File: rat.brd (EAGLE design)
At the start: 102.5 x 80 mm, 64 parts, among them J1 B2B-PH-K-S(LF)(SN), J2 B2B-PH-K-S(LF)(SN), J3 PPTC041LFBN-RC, J4 PPTC081LFBN-RCCONN_PPTC081LFB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, Q1A SFH_313_FA-3/4, Q1B SFH_313_FA-3/4, Q1C SFH_313_FA-3/4, Q1D SFH_313_FA-3/4, Q2A Q2, Q2B Q2, Q2C Q2, Q2D Q2, U1 L293DD, U2 LD1117D33CTR, U3 STM32F205RGT6

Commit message: Some Routing Done
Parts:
- moved R3A 25.3 mm to (78.1, 67.9), turned to 180 degrees
- moved R3C 23.4 mm to (80.0, 29.2), turned to 270 degrees
- moved C13 21.5 mm to (35.6, 9.53), turned to 0 degrees
- moved S1 18.7 mm to (19.7, 31.8), turned to 180 degrees
- moved R5 14.3 mm to (50.2, 22.7), turned to 90 degrees
- moved RIGHT 13.2 mm to (56.4, 72.8), turned to 180 degrees
- moved R2C 10.6 mm to (47.6, 23.2)
- moved R6 7.01 mm to (61.6, 51.4), turned to 90 degrees
- moved C11 6.35 mm to (63.5, 45.7), turned to 180 degrees
- moved R4C 5.85 mm to (87.6, 27.3), turned to 180 degrees
- moved C8D 5.75 mm to (18.4, 61.6), turned to 90 degrees
- moved Q2D 5.68 mm to (76.2, 15.2)
- moved R1D 5.68 mm to (43.2, 22.9), turned to 90 degrees
- moved R3D 5.12 mm to (66.7, 36.8), turned to 180 degrees
- moved R4D 4.02 mm to (68.6, 15.2), turned to 90 degrees
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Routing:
- net N$14: track 0.00 -> 61.2 mm, vias 0 -> 2
- net PC7: track 0.00 -> 60.6 mm
- net VBAT: track 0.00 -> 59.9 mm
- net VCC: track 0.00 -> 53.9 mm
- net PB6: track 0.00 -> 36.2 mm, vias 0 -> 2
- net N$8: track 0.00 -> 34.9 mm
- net PB8: track 0.00 -> 32.7 mm, vias 0 -> 2
- net N$17: track 0.00 -> 28.4 mm
- net N$2: track 0.00 -> 26.4 mm
- net PB10: track 0.00 -> 25.7 mm
- net PB11: track 0.00 -> 25.5 mm
- net N$5: track 0.00 -> 22.7 mm
- net N$3: track 0.00 -> 22.1 mm
- net PB7: track 0.00 -> 18.7 mm, vias 0 -> 2
- net N$4: track 0.00 -> 18.6 mm
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- added copper zone on layer 1, net VCC
- removed copper zone on layer 1, net VBAT

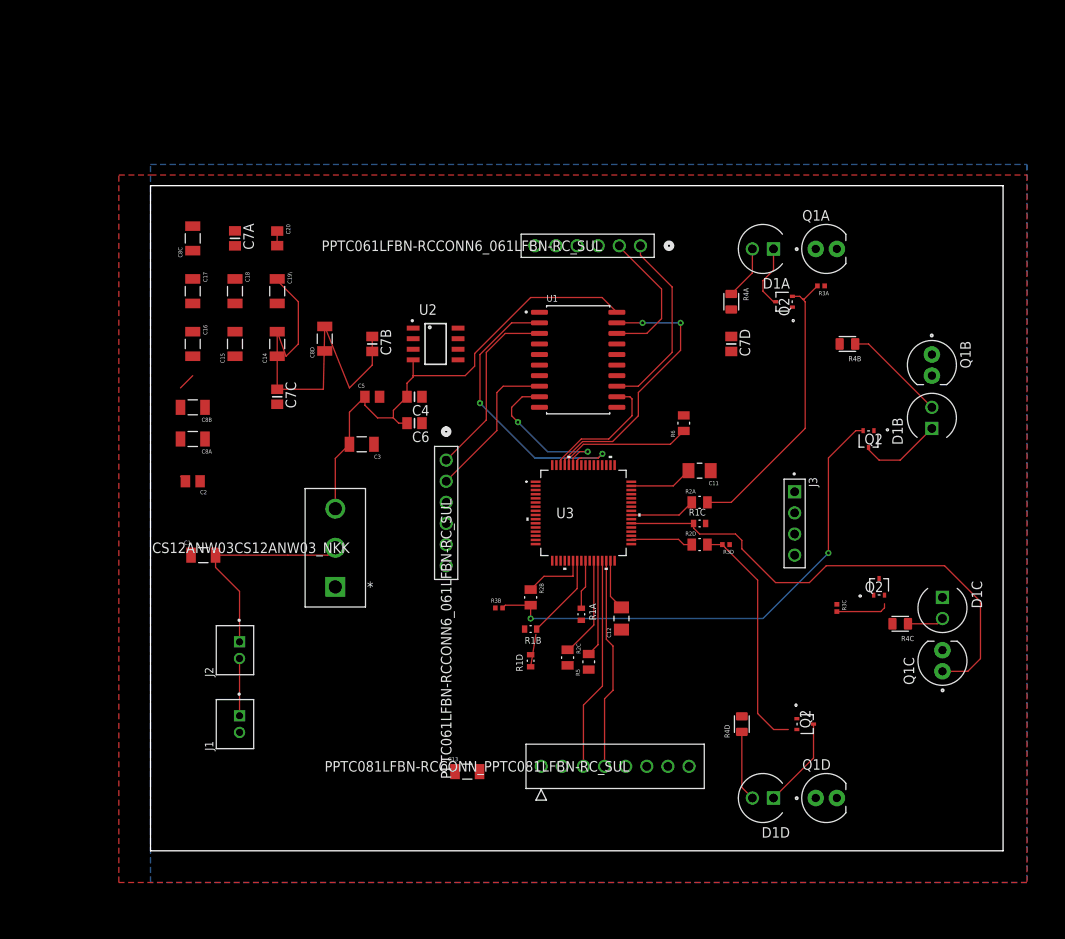
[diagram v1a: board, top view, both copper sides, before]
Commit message: Airwires eliminated
Restriction problems still remain; not sure why I can't route under components
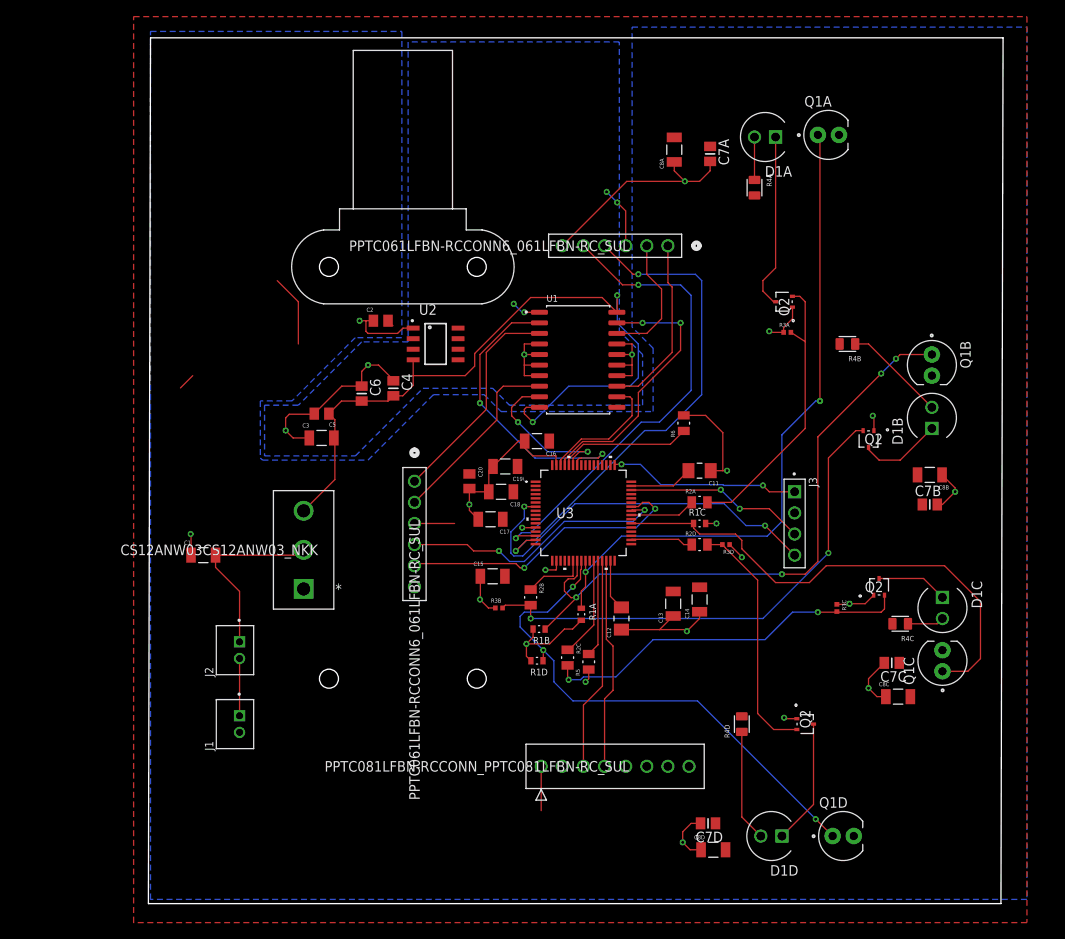
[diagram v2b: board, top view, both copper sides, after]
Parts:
- added U$1, U$2: MOTOR, micromouseMotors:MOTOR
- moved C8C 101.2 mm to (87.4, 18.5), turned to 0 degrees
- moved C8B 89.0 mm to (91.2, 45.2)
- moved C7C 80.5 mm to (86.6, 22.6), turned to 180 degrees
- moved C8D 77.2 mm to (65.2, 0.13), turned to 0 degrees
- moved C7B 69.8 mm to (91.2, 41.7), turned to 0 degrees
- moved C8A 67.6 mm to (60.5, 84.3), turned to 90 degrees
- moved C14 59.4 mm to (63.5, 30.2)
- moved C7A 58.0 mm to (64.8, 83.8)
- moved C7D 57.7 mm to (64.5, 3.30), turned to 180 degrees
- moved C17 45.1 mm to (38.4, 39.9), turned to 180 degrees
- moved C16 43.0 mm to (43.9, 49.3), turned to 180 degrees
- moved C15 41.7 mm to (38.6, 33.0), turned to 0 degrees
- moved C18 40.1 mm to (39.6, 43.2), turned to 180 degrees
- moved C20 37.2 mm to (35.8, 44.5)
- moved C19\ 34.6 mm to (40.1, 46.2), turned to 180 degrees
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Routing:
- net GND: track 0.00 -> 141.6 mm, vias 0 -> 20
- net PC5: track 5.93 -> 80.9 mm, vias 0 -> 2
- net PA7: track 10.2 -> 75.5 mm, vias 0 -> 4
- net PA1: track 0.00 -> 60.2 mm, vias 0 -> 2
- net PC4: track 3.95 -> 63.4 mm, vias 0 -> 3
- net PA0: track 0.00 -> 57.8 mm, vias 0 -> 2
- net NRST: track 0.00 -> 47.1 mm, vias 0 -> 2
- net MGND: track 0.00 -> 44.4 mm, vias 0 -> 4
- net N$10: track 6.41 -> 45.0 mm, vias 0 -> 2
- net PA9: track 0.00 -> 35.6 mm, vias 0 -> 2
- net PA8: track 0.00 -> 32.8 mm, vias 0 -> 2
- net VBAT: track 59.9 -> 90.4 mm, vias 0 -> 2
- net SWCLK: track 0.00 -> 23.1 mm, vias 0 -> 2
- net SWDIO: track 0.00 -> 21.9 mm, vias 0 -> 2
- net VCC: track 53.9 -> 32.7 mm, vias 0 -> 5
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- added copper zone on layer 16, net MGND
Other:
- board size 102.5 x 80 mm -> 102.8 x 104.1 mm

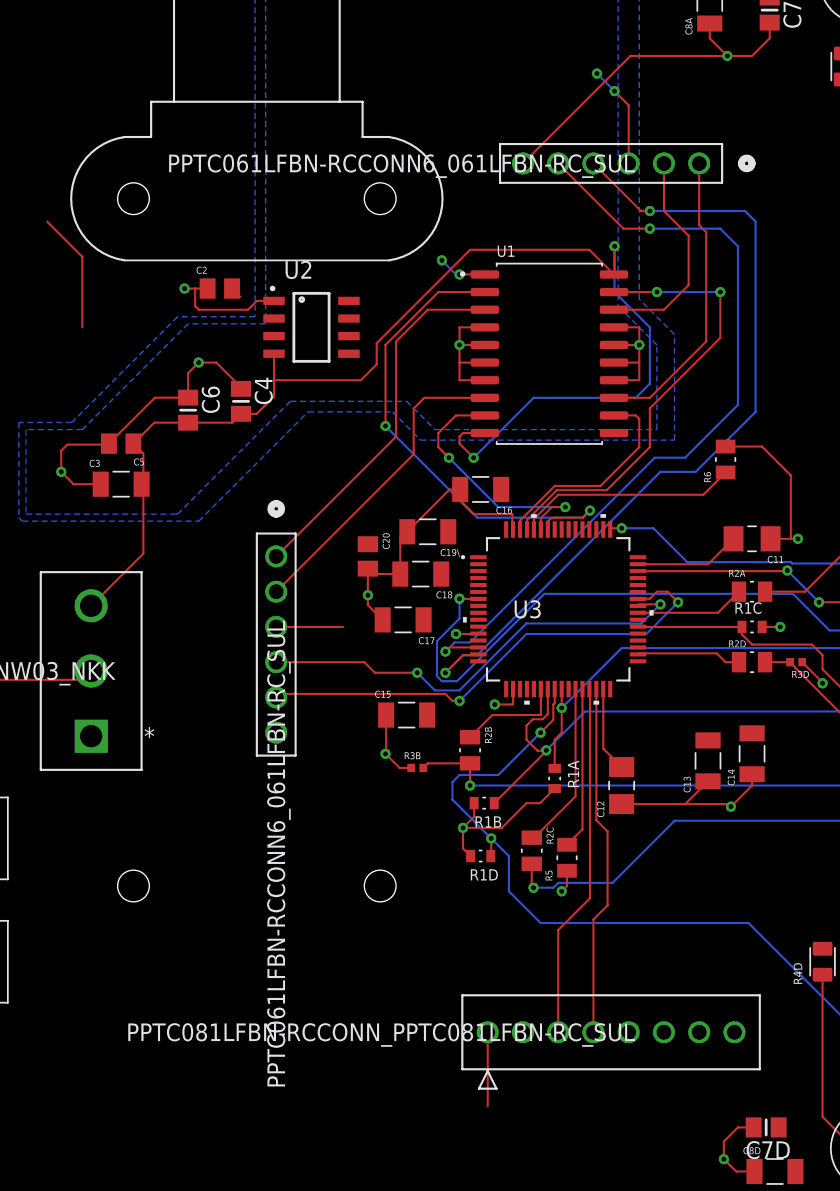
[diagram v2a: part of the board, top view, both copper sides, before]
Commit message: Made Power Signals 45mil Trace
Still need to make analog signals 15mil trace
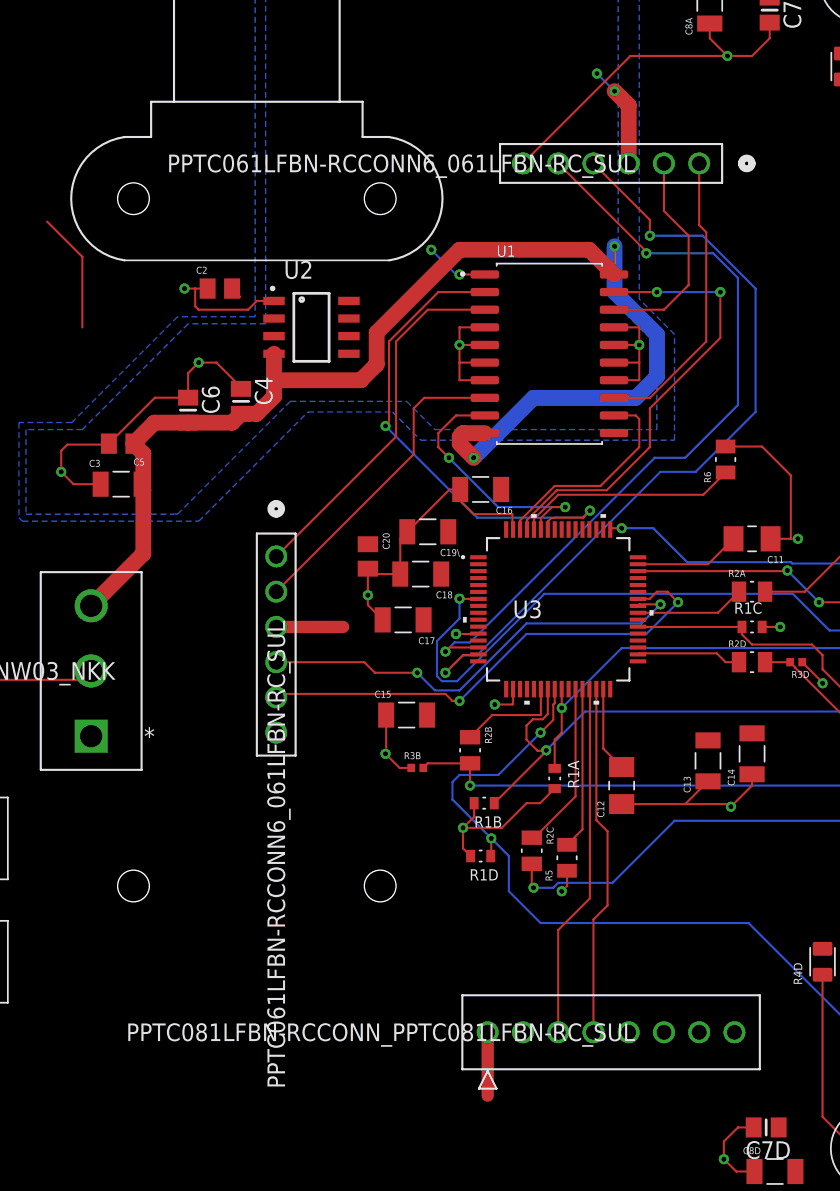
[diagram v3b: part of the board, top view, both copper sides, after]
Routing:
- net PA1: track 60.2 -> 58.0 mm
- net PA0: track 57.8 -> 56.5 mm
- net VBAT: track 90.4 -> 91.3 mm
- net VCC: track 32.7 -> 33.0 mm, vias 5 -> 4
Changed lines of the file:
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@@
 <via x="42.418" y="64.77" extent="1-16" drill="0.35"/>
 <wire x1="42.418" y1="64.77" x2="42.164" y2="64.77" width="0.1524" layer="16"/>
-<wire x1="42.164" y1="64.77" x2="41.148" y2="65.786" width="0.1524" layer="16"/>
-<via x="41.148" y="65.786" extent="1-16" drill="0.35"/>
-<wire x1="54.61" y1="72.771" x2="54.61" y2="76.962" width="0.1524" layer="1"/>
-<wire x1="54.61" y1="76.962" x2="53.594" y2="77.978" width="0.1524" layer="1"/>
+<wire x1="42.164" y1="64.77" x2="40.386" y2="66.548" width="0.1524" layer="16"/>
+<via x="40.386" y="66.548" extent="1-16" drill="0.35"/>
+<wire x1="54.61" y1="72.771" x2="54.61" y2="76.962" width="1.143" layer="1"/>
+<wire x1="54.61" y1="76.962" x2="53.594" y2="77.978" width="1.143" layer="1"/>
 <via x="53.594" y="77.978" extent="1-16" drill="0.35"/>
 <wire x1="53.594" y1="77.978" x2="52.324" y2="79.248" width="0.1524" layer="16"/>
 <via x="52.324" y="79.248" extent="1-16" drill="0.35"/>
-<via x="44.45" y="10.16" extent="1-16" drill="0.35"/>
-<wire x1="44.45" y1="10.16" x2="44.45" y2="4.826" width="0.1524" layer="1"/>
-<wire x1="29.21" y1="39.37" x2="34.036" y2="39.37" width="0.1524" layer="1"/>
+<wire x1="29.21" y1="39.37" x2="34.036" y2="39.37" width="0.889" layer="1"/>
+<wire x1="44.45" y1="10.16" x2="44.45" y2="5.588" width="0.889" layer="1"/>
 </signal>
 <signal name="N$3">
@@
 <contactref element="U3" pad="58"/>
 <wire x1="44.24" y1="63.5" x2="40.894" y2="63.5" width="0.1524" layer="1"/>
-<wire x1="40.894" y1="63.5" x2="37.084" y2="59.69" width="0.1524" layer="1"/>
-<wire x1="37.084" y1="59.69" x2="37.084" y2="53.848" width="0.1524" layer="1"/>
+<wire x1="40.894" y1="63.5" x2="37.338" y2="59.944" width="0.1524" layer="1"/>
+<wire x1="37.338" y1="59.944" x2="37.338" y2="54.102" width="0.1524" layer="1"/>
+<wire x1="37.338" y1="54.102" x2="37.084" y2="53.848" width="0.1524" layer="1"/>
 <wire x1="49.0329125" y1="47.2155" x2="49.2475" y2="47.2155" width="0.1524" layer="1"/>
 <wire x1="49.2475" y1="47.2155" x2="49.276" y2="47.244" width="0.1524" layer="1"/>
@@
 <contactref element="C4" pad="2"/>
 <contactref element="C6" pad="2"/>
-<wire x1="19.633434375" y1="49.2246125" x2="19.633434375" y2="44.652434375" width="0.1524" layer="1"/>
-<wire x1="15.875" y1="40.894" x2="19.633434375" y2="44.652434375" width="0.1524" layer="1"/>
+<wire x1="19.633434375" y1="49.2246125" x2="19.633434375" y2="44.652434375" width="1.143" layer="1"/>
+<wire x1="15.875" y1="40.894" x2="19.633434375" y2="44.652434375" width="1.143" layer="1"/>
 <wire x1="19.633434375" y1="49.2246125" x2="19.509" y2="49.657" width="0.1524" layer="1"/>
-<wire x1="29.05" y1="55.974" x2="27.802" y2="54.726" width="0.1524" layer="1"/>
-<wire x1="26.67" y1="54.726" x2="27.802" y2="54.726" width="0.1524" layer="1"/>
-<wire x1="53.55" y1="64.77" x2="51.772" y2="66.548" width="0.1524" layer="1"/>
-<wire x1="51.772" y1="66.548" x2="43.18" y2="66.548" width="0.1524" layer="1"/>
-<wire x1="43.18" y1="66.548" x2="36.449" y2="59.817" width="0.1524" layer="1"/>
-<wire x1="36.449" y1="59.817" x2="36.449" y2="58.293" width="0.1524" layer="1"/>
-<wire x1="35.306" y1="57.15" x2="29.05" y2="57.15" width="0.1524" layer="1"/>
-<wire x1="36.449" y1="58.293" x2="35.306" y2="57.15" width="0.1524" layer="1"/>
-<wire x1="26.67" y1="54.726" x2="26.035" y2="54.091" width="0.1524" layer="1"/>
-<wire x1="26.035" y1="54.091" x2="22.86" y2="54.091" width="0.1524" layer="1"/>
-<wire x1="18.914" y1="52.578" x2="20.427" y2="54.091" width="0.1524" layer="1"/>
-<wire x1="20.427" y1="54.091" x2="22.86" y2="54.091" width="0.1524" layer="1"/>
-<wire x1="18.914" y1="52.578" x2="19.633434375" y2="51.858565625" width="0.1524" layer="1"/>
-<wire x1="19.633434375" y1="51.858565625" x2="19.633434375" y2="49.2246125" width="0.1524" layer="1"/>
-<wire x1="29.05" y1="59.055" x2="29.05" y2="57.15" width="0.1524" layer="1"/>
-<wire x1="29.05" y1="57.15" x2="29.05" y2="55.974" width="0.1524" layer="1"/>
-<wire x1="44.24" y1="53.34" x2="42.672" y2="53.34" width="0.1524" layer="1"/>
-<wire x1="42.672" y1="53.34" x2="42.418" y2="53.086" width="0.1524" layer="1"/>
+<wire x1="29.05" y1="55.974" x2="27.802" y2="54.726" width="1.143" layer="1"/>
+<wire x1="26.67" y1="54.726" x2="27.802" y2="54.726" width="1.143" layer="1"/>
+<wire x1="53.55" y1="64.77" x2="51.772" y2="66.548" width="1.143" layer="1"/>
+<wire x1="51.772" y1="66.548" x2="42.418" y2="66.548" width="1.143" layer="1"/>
+<wire x1="42.418" y1="66.548" x2="36.449" y2="60.579" width="1.143" layer="1"/>
+<wire x1="36.449" y1="60.579" x2="36.449" y2="58.293" width="1.143" layer="1"/>
+<wire x1="35.306" y1="57.15" x2="29.05" y2="57.15" width="1.143" layer="1"/>
+<wire x1="36.449" y1="58.293" x2="35.306" y2="57.15" width="1.143" layer="1"/>
+<wire x1="26.67" y1="54.726" x2="26.035" y2="54.091" width="1.143" layer="1"/>
+<wire x1="26.035" y1="54.091" x2="22.86" y2="54.091" width="1.143" layer="1"/>
+<wire x1="18.914" y1="52.578" x2="20.427" y2="54.091" width="1.143" layer="1"/>
+<wire x1="20.427" y1="54.091" x2="22.86" y2="54.091" width="1.143" layer="1"/>
+<wire x1="18.914" y1="52.578" x2="19.633434375" y2="51.858565625" width="1.143" layer="1"/>
+<wire x1="19.633434375" y1="51.858565625" x2="19.633434375" y2="49.2246125" width="1.143" layer="1"/>
+<wire x1="29.05" y1="59.055" x2="29.05" y2="57.15" width="1.143" layer="1"/>
+<wire x1="29.05" y1="57.15" x2="29.05" y2="55.974" width="1.143" layer="1"/>
+<wire x1="44.24" y1="53.34" x2="42.672" y2="53.34" width="1.143" layer="1"/>
+<wire x1="42.672" y1="53.34" x2="42.418" y2="53.086" width="1.143" layer="1"/>
 <wire x1="42.418" y1="53.086" x2="42.418" y2="52.578" width="0.1524" layer="1"/>
-<wire x1="42.418" y1="52.578" x2="43.434" y2="51.562" width="0.1524" layer="1"/>
+<wire x1="42.418" y1="52.578" x2="43.434" y2="51.562" width="1.143" layer="1"/>
 <via x="43.434" y="51.562" extent="1-16" drill="0.35"/>
-<wire x1="43.434" y1="51.562" x2="47.752" y2="55.88" width="0.1524" layer="16"/>
+<wire x1="43.434" y1="51.562" x2="47.752" y2="55.88" width="1.143" layer="16"/>
 <via x="53.594" y="66.802" extent="1-16" drill="0.35"/>
 <wire x1="53.594" y1="66.802" x2="53.594" y2="64.814" width="0.1524" layer="1"/>
 <wire x1="53.594" y1="64.814" x2="53.55" y2="64.77" width="0.1524" layer="1"/>
-<wire x1="55.118" y1="55.88" x2="56.134" y2="56.896" width="0.1524" layer="16"/>
-<wire x1="56.134" y1="56.896" x2="56.134" y2="60.96" width="0.1524" layer="16"/>
-<wire x1="53.594" y1="63.5" x2="53.594" y2="66.802" width="0.1524" layer="16"/>
-<wire x1="47.752" y1="55.88" x2="55.118" y2="55.88" width="0.1524" layer="16"/>
-<wire x1="56.134" y1="60.96" x2="53.594" y2="63.5" width="0.1524" layer="16"/>
+<wire x1="55.118" y1="55.88" x2="56.642" y2="57.404" width="1.143" layer="16"/>
+<wire x1="56.642" y1="57.404" x2="56.642" y2="60.452" width="1.143" layer="16"/>
+<wire x1="53.594" y1="63.5" x2="53.594" y2="66.802" width="1.143" layer="16"/>
+<wire x1="47.752" y1="55.88" x2="55.118" y2="55.88" width="1.143" layer="16"/>
+<wire x1="56.642" y1="60.452" x2="53.594" y2="63.5" width="1.143" layer="16"/>
 </signal>
 <signal name="N$26">
@@
 <wire x1="42.0652" y1="38.2552" x2="43.17735" y2="38.2552" width="0.1524" layer="16"/>
 <wire x1="43.17735" y1="38.2552" x2="56.48415" y2="51.562" width="0.1524" layer="16"/>
-<wire x1="62.484" y1="55.372" x2="58.674" y2="51.562" width="0.1524" layer="16"/>
-<via x="56.134" y="68.072" extent="1-16" drill="0.35"/>
-<wire x1="49.53" y1="72.771" x2="54.229" y2="68.072" width="0.1524" layer="1"/>
-<wire x1="54.229" y1="68.072" x2="56.134" y2="68.072" width="0.1524" layer="1"/>
-<wire x1="61.214" y1="68.072" x2="62.484" y2="66.802" width="0.1524" layer="16"/>
-<wire x1="62.484" y1="66.802" x2="62.484" y2="55.372" width="0.1524" layer="16"/>
-<wire x1="56.134" y1="68.072" x2="61.214" y2="68.072" width="0.1524" layer="16"/>
+<wire x1="58.674" y1="51.562" x2="62.484" y2="55.372" width="0.1524" layer="16"/>
+<via x="55.88" y="66.294" extent="1-16" drill="0.35"/>
+<wire x1="62.484" y1="55.372" x2="62.484" y2="64.516" width="0.1524" layer="16"/>
+<wire x1="62.484" y1="64.516" x2="60.706" y2="66.294" width="0.1524" layer="16"/>
+<wire x1="60.706" y1="66.294" x2="55.88" y2="66.294" width="0.1524" layer="16"/>
+<wire x1="49.53" y1="72.771" x2="55.88" y2="66.421" width="0.1524" layer="1"/>
+<wire x1="55.88" y1="66.421" x2="55.88" y2="66.294" width="0.1524" layer="1"/>
 </signal>
 <signal name="PA1">
@@
 <wire x1="43.688" y1="37.338" x2="56.896" y2="50.546" width="0.1524" layer="16"/>
 <wire x1="59.436" y1="50.546" x2="63.754" y2="54.864" width="0.1524" layer="16"/>
-<wire x1="63.754" y1="54.864" x2="63.754" y2="68.58" width="0.1524" layer="16"/>
-<wire x1="63.754" y1="68.58" x2="62.992" y2="69.342" width="0.1524" layer="16"/>
-<wire x1="62.992" y1="69.342" x2="56.134" y2="69.342" width="0.1524" layer="16"/>
-<via x="56.134" y="69.342" extent="1-16" drill="0.35"/>
+<via x="56.134" y="67.564" extent="1-16" drill="0.35"/>
 <wire x1="56.896" y1="50.546" x2="59.436" y2="50.546" width="0.1524" layer="16"/>
-<wire x1="52.07" y1="72.771" x2="55.499" y2="69.342" width="0.1524" layer="1"/>
-<wire x1="55.499" y1="69.342" x2="56.134" y2="69.342" width="0.1524" layer="1"/>
+<wire x1="63.754" y1="54.864" x2="63.754" y2="63.754" width="0.1524" layer="16"/>
+<wire x1="63.754" y1="63.754" x2="59.944" y2="67.564" width="0.1524" layer="16"/>
+<wire x1="59.944" y1="67.564" x2="56.134" y2="67.564" width="0.1524" layer="16"/>
+<wire x1="52.07" y1="72.771" x2="56.134" y2="68.707" width="0.1524" layer="1"/>
+<wire x1="56.134" y1="68.707" x2="56.134" y2="67.564" width="0.1524" layer="1"/>
 </signal>
 <signal name="PA9">
